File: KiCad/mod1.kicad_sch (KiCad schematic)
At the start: 67 parts, among them M1 Fan_4pin, M2 Fan_4pin, U1 ZD25Q64BSIGT

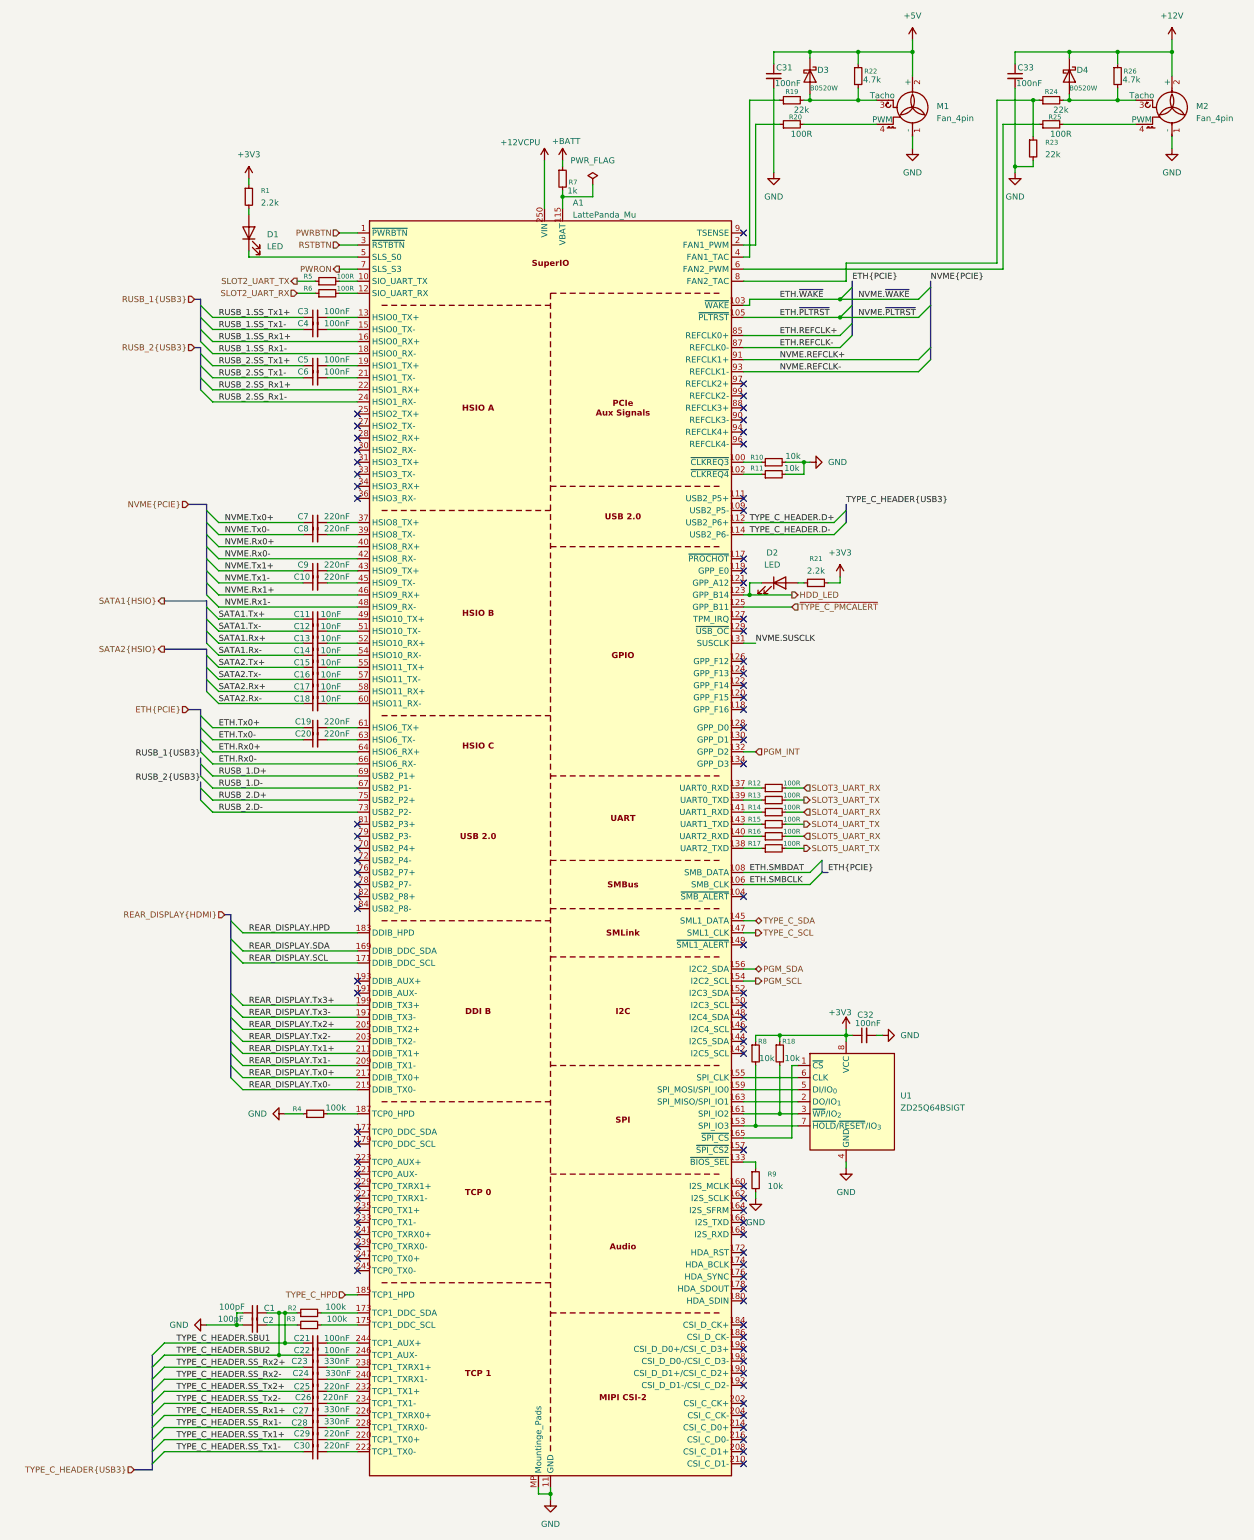
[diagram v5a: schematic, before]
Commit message: Finish fixing footprints
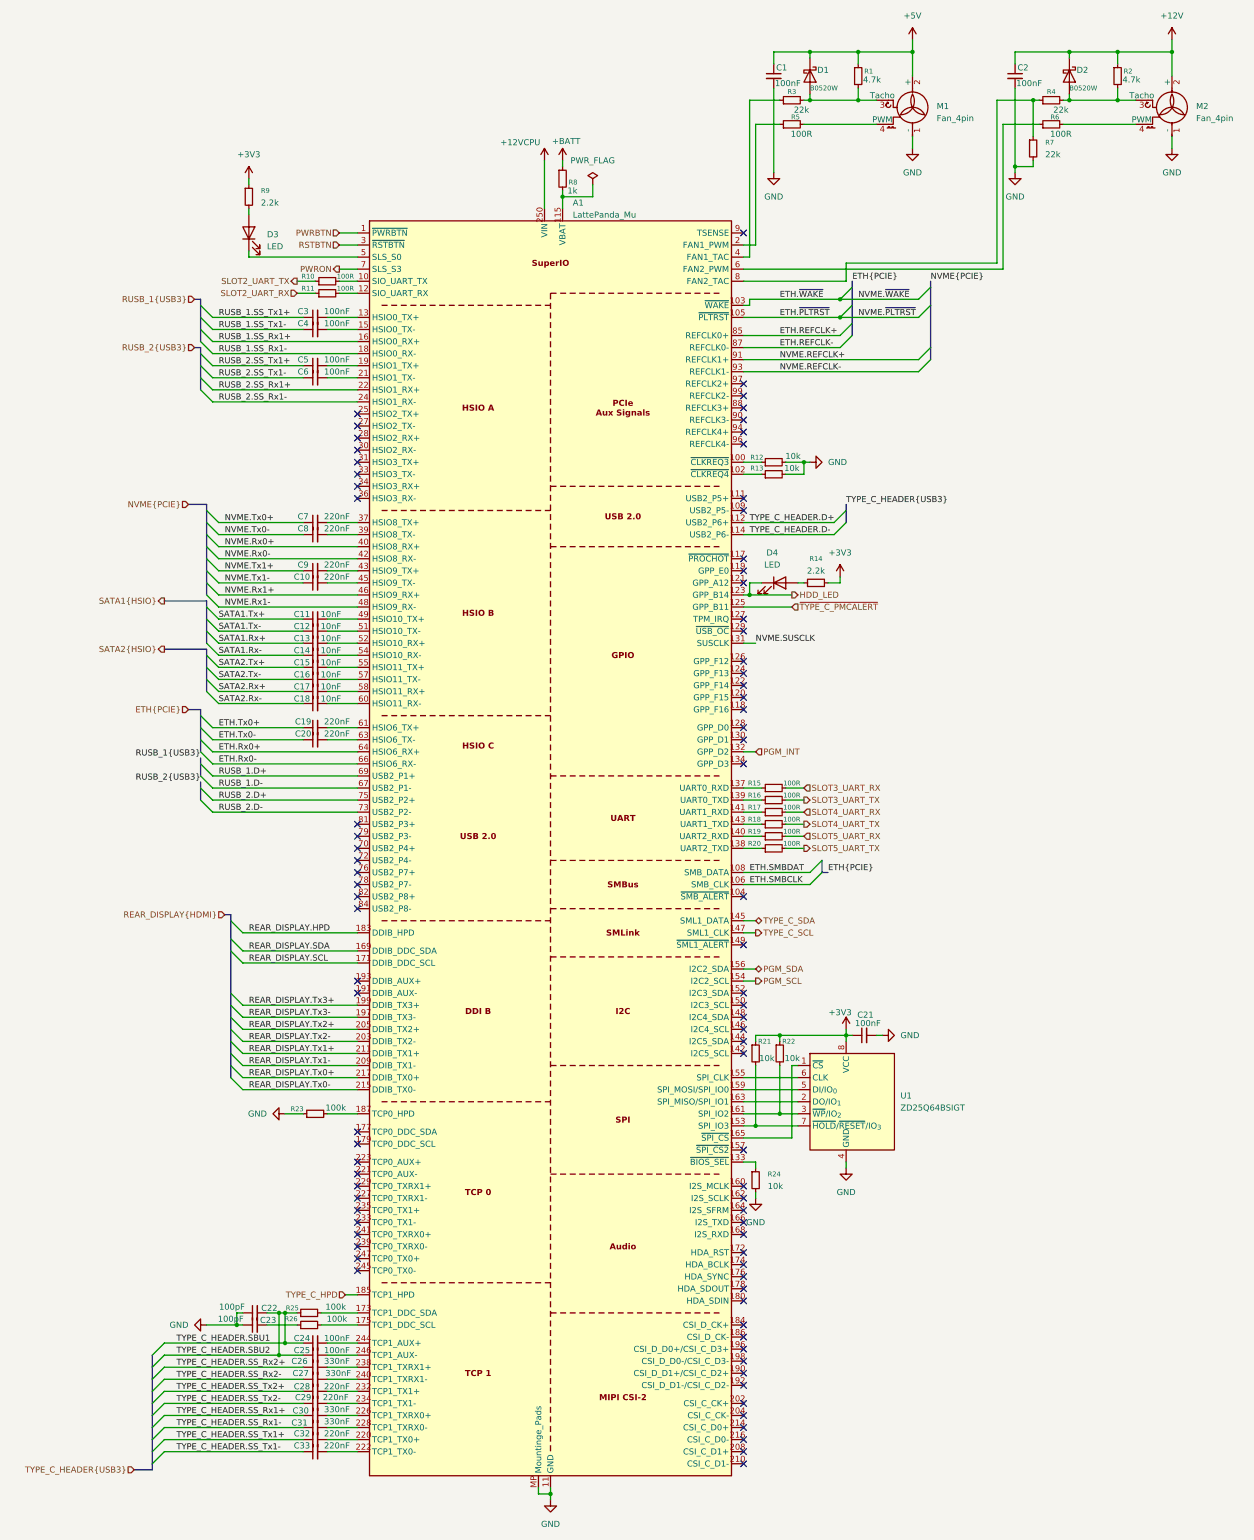
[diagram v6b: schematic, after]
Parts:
- renumbered C31 to C1, C33 to C2, C32 to C21, C1 to C22, C2 to C23, C21 to C24, C22 to C25, C23 to C26, C24 to C27, C25 to C28, C26 to C29, C27 to C30, C28 to C31, C29 to C32, C30 to C33, D3 to D1, D4 to D2, D1 to D3, D2 to D4, R22 to R1, R5 to R10, R6 to R11, R10 to R12, R11 to R13, R21 to R14, R12 to R15, R13 to R16, R14 to R17, R15 to R18, R16 to R19, R26 to R2, R17 to R20, R8 to R21, R18 to R22, R4 to R23, R9 to R24, R2 to R25, R3 to R26, R19 to R3, R24 to R4, R20 to R5, R25 to R6, R23 to R7, R7 to R8, R1 to R9

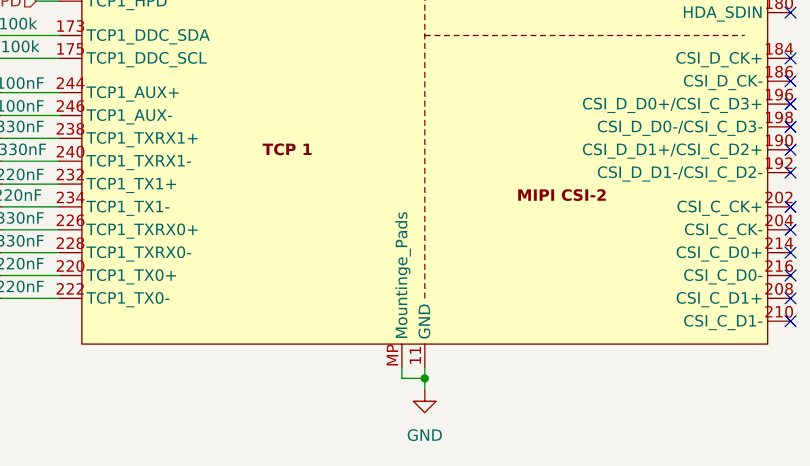
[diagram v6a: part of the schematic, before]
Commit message: Fix more footprint issues, continue laying out components
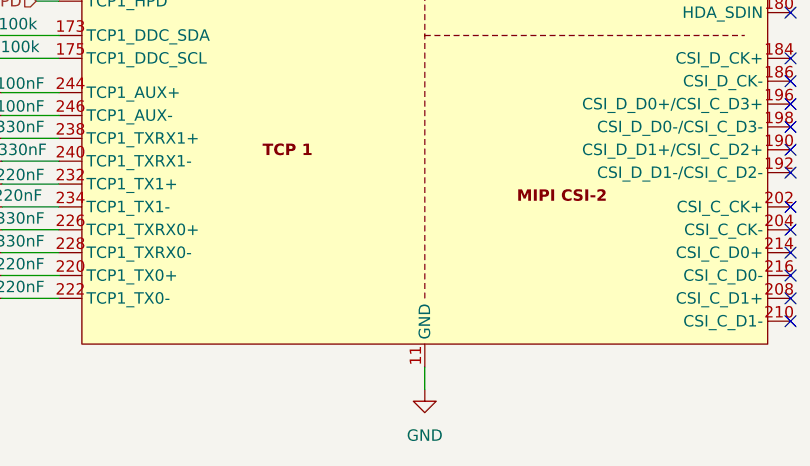
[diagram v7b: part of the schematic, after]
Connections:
- net GND: no longer A1.MP (Mountinge_Pads)
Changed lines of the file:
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@@
 	)
 	(junction
-		(at 284.48 345.44)
-		(diameter 0)
-		(color 0 0 0 0)
-	)
-	(junction
 		(at 346.71 248.92)
 		(diameter 0)
@@
 	(wire
 		(pts
-			(xy 281.94 345.44) (xy 284.48 345.44)
-		)
-		(stroke
-			(width 0)
-			(type default)
-		)
-	)
-	(wire
-		(pts
 			(xy 325.12 128.27) (xy 328.93 128.27)
 		)
@@
 	(wire
 		(pts
-			(xy 284.48 345.44) (xy 284.48 346.71)
+			(xy 284.48 344.17) (xy 284.48 346.71)
 		)
 		(stroke
@@
 	(wire
 		(pts
-			(xy 284.48 344.17) (xy 284.48 345.44)
-		)
-		(stroke
-			(width 0)
-			(type default)
-		)
-	)
-	(wire
-		(pts
 			(xy 220.98 68.58) (xy 220.98 69.85)
 		)
@@
 		)
 	)
-	(wire
-		(pts
-			(xy 281.94 344.17) (xy 281.94 345.44)
-		)
-		(stroke
-			(width 0)
-			(type default)
-		)
-	)
 	(bus
 		(pts
@@
 		(pin "230"
 		)
-		(pin "MP"
-		)
 		(pin "157"

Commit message: Place STM32 and fix cpu fan headers
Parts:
- M1: footprint Connector:FanPinHeader_1x04_P2.54mm_Vertical -> Connector_JST:JST_PH_B4B-PH-K_1x04_P2.00mm_Vertical
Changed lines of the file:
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@@
 			)
 		)
-		(property "Footprint" "Connector:FanPinHeader_1x04_P2.54mm_Vertical"
+		(property "Footprint" "Connector_JST:JST_PH_B4B-PH-K_1x04_P2.00mm_Vertical"
 			(at 360.68 54.356 0)
 			(effects
